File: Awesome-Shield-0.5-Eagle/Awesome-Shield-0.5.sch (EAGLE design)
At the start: 13 parts, among them J1 ARDUINO_R3_SHIELDUNO_R3_SHIEL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, J2 TWIG_2.0, J3 TWIG_2.0, SW1 SPST_TACT-EVQQ2

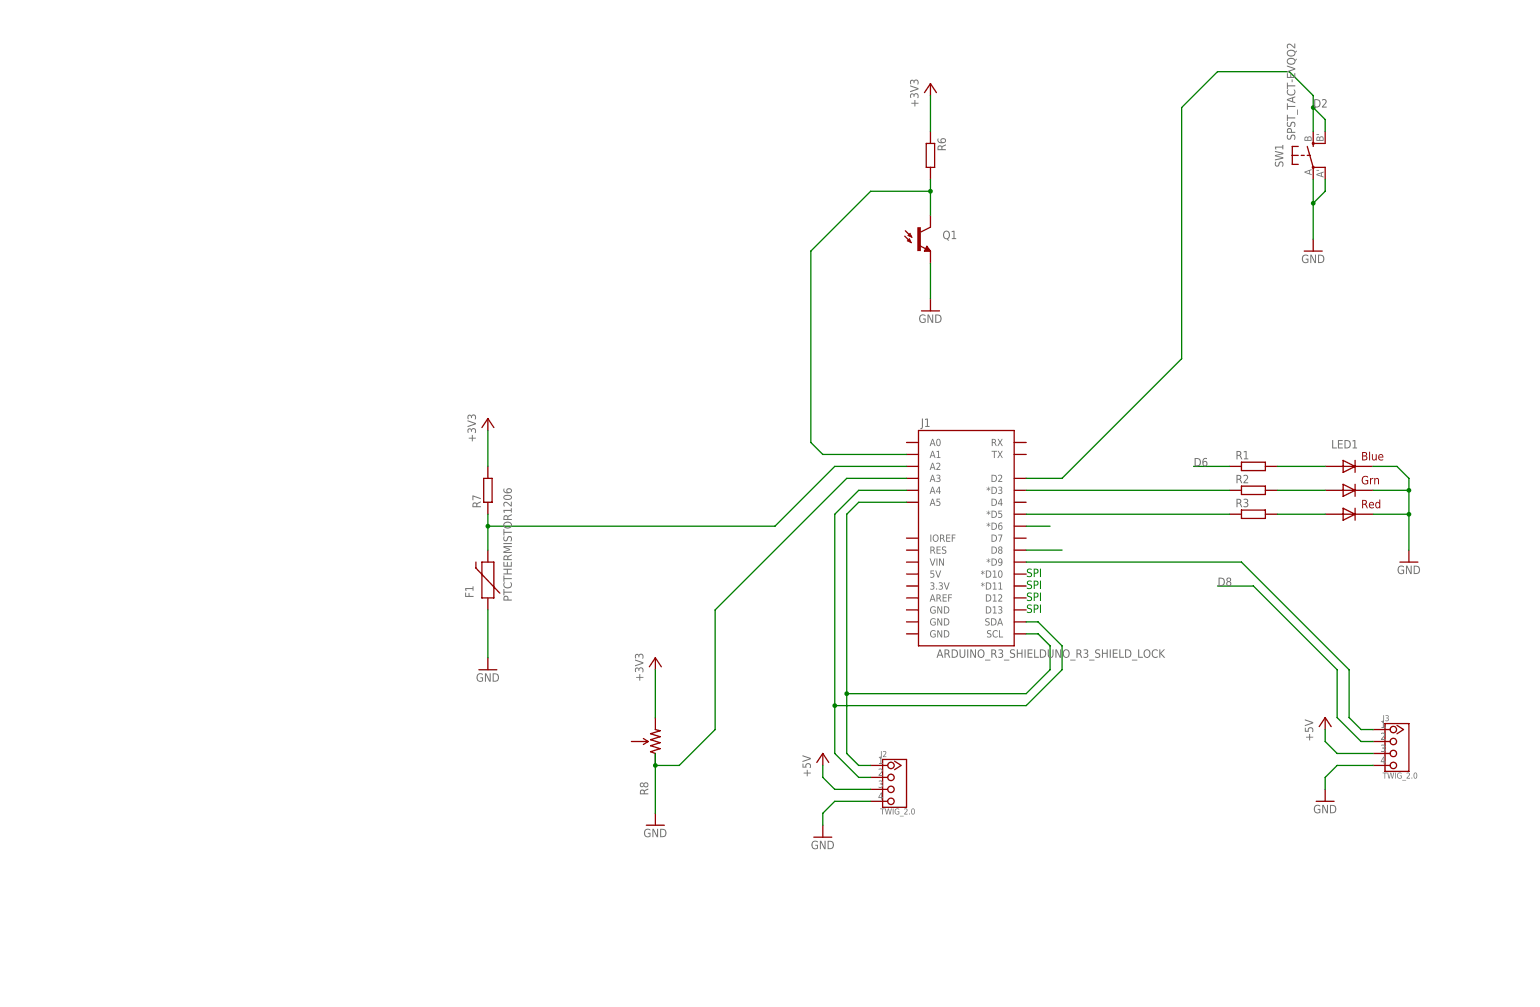
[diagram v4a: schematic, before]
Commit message: added 3rd grove port
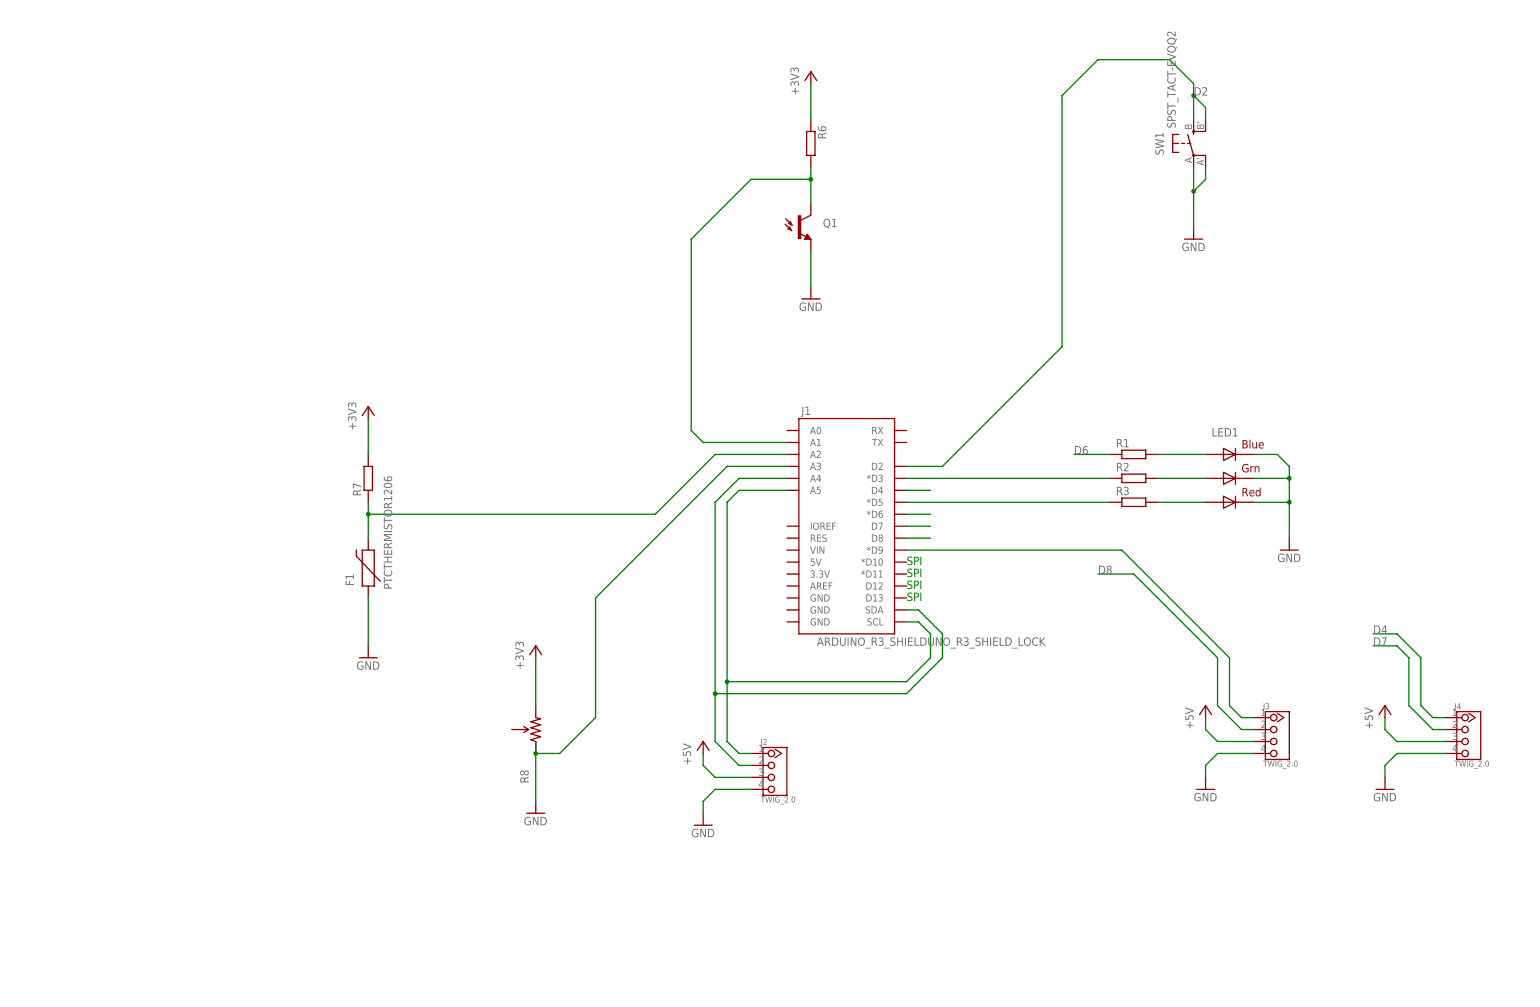
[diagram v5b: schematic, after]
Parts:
- added J4: TWIG_2.0, CONNECTER:TWIG_2.0
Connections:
- new net D4: J1.D4, J4.1
- new net D7: J1.D7, J4.2
- net +5V: now also J4.3
- net GND: now also J4.4
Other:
- moved on the sheet: F1, J1, J2, J3, LED1, Q1, R1, R2, R3, R6, R7, R8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

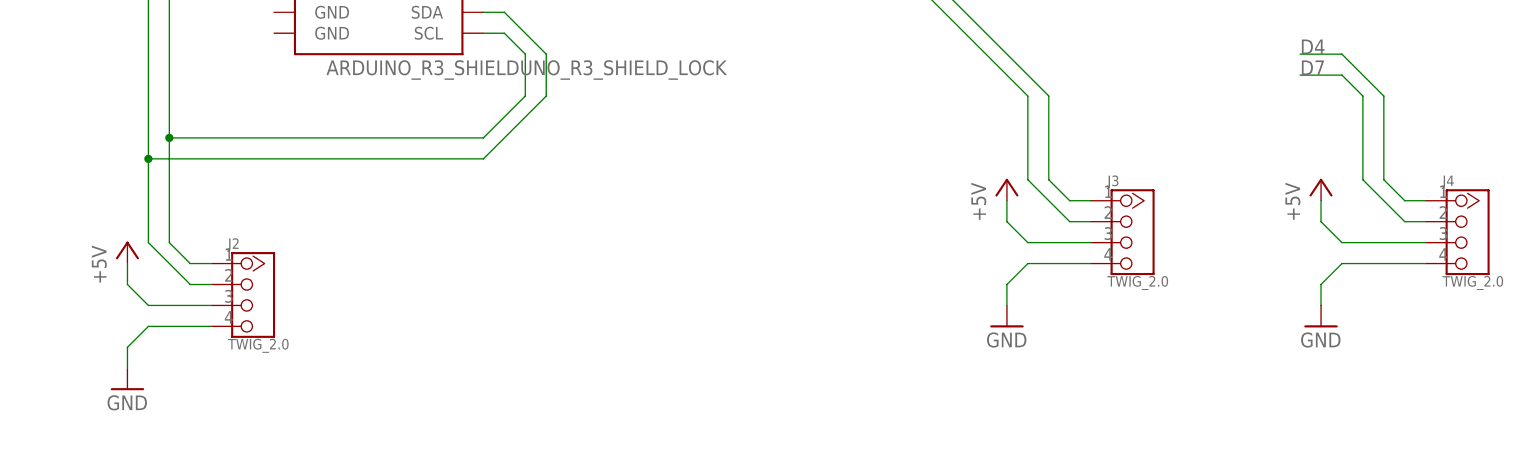
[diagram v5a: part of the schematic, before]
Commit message: changed grove ports to SMT
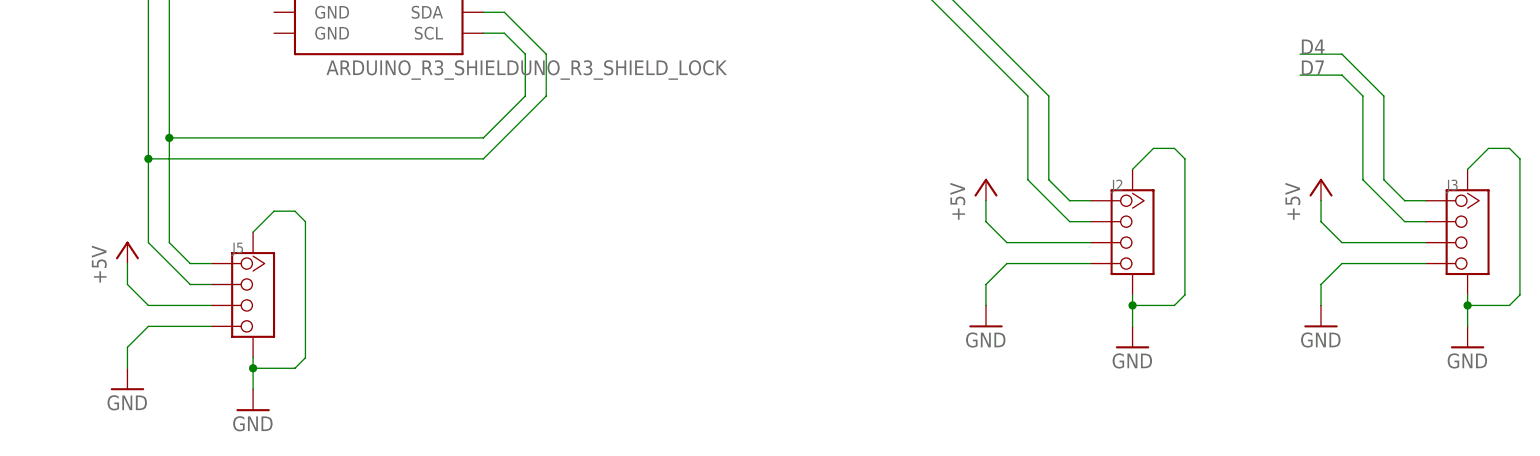
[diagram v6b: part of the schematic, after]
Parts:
- removed J4: TWIG_2.0, CONNECTER:TWIG_2.0
- added J5: (no value), Connector :TWIG-4P-2.0-SMD-FEMALE-REINFORCE'DD'
- J2, J3: value TWIG_2.0 -> (none); device CONNECTER:TWIG_2.0 -> Connector :TWIG-4P-2.0-SMD-FEMALE-REINFORCE'DD'
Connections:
- net +5V: now also J5.3; no longer J4.3
- net A4: now also J5.2; no longer J2.2
- net A5: now also J5.1; no longer J2.1
- net D4: now also J3.1; no longer J4.1
- net D7: now also J3.2; no longer J4.2
- net D8: now also J2.2; no longer J3.2
- net GND: now also J2.SS1, J2.SS2, J3.SS1, J3.SS2, J5.4, J5.SS1, J5.SS2; no longer J4.4
- net N$2: now also J2.1; no longer J3.1
